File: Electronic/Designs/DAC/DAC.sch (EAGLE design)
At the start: 37 parts

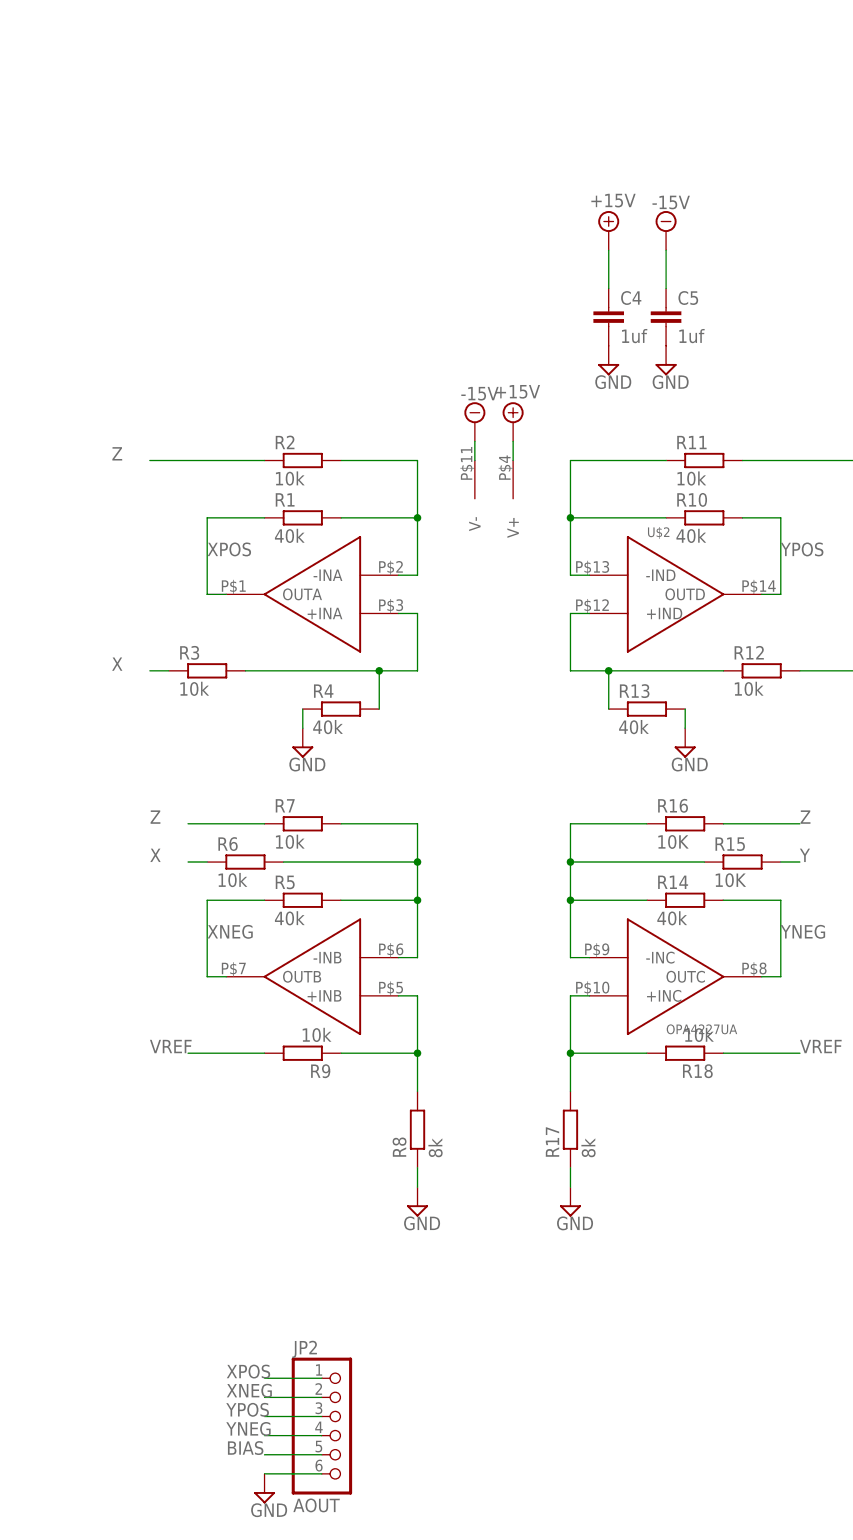
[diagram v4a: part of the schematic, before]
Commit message: improved dac board layout
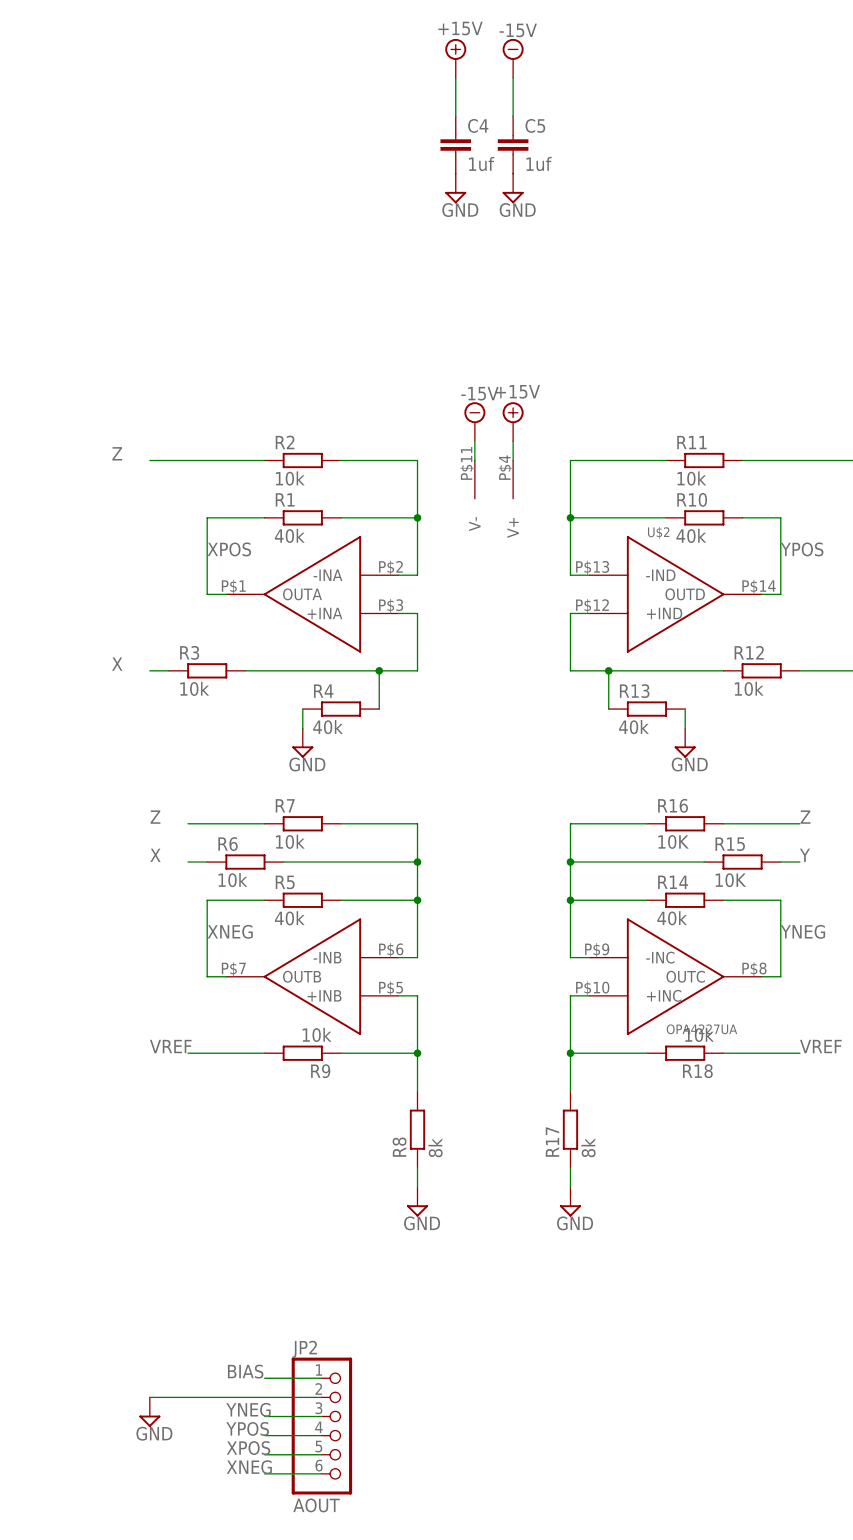
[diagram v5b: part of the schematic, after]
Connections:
- net BIAS: now also JP2.1; no longer JP2.5
- net GND: now also JP2.2; no longer JP2.6
- net XNEG: now also JP2.6; no longer JP2.2
- net XPOS: now also JP2.5; no longer JP2.1
- net YNEG: now also JP2.3; no longer JP2.4
- net YPOS: now also JP2.4; no longer JP2.3
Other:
- moved on the sheet: C4, C5
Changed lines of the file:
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@@
 <instance part="SUPPLY9" gate="GND" x="38.1" y="-50.8"/>
 <instance part="JP2" gate="A" x="99.06" y="-99.06"/>
-<instance part="SUPPLY10" gate="GND" x="88.9" y="-106.68"/>
+<instance part="SUPPLY10" gate="GND" x="73.66" y="-96.52"/>
 <instance part="JP3" gate="A" x="-50.8" y="0" rot="R180"/>
 <instance part="SUPPLY11" gate="GND" x="-40.64" y="-15.24"/>
@@
 <instance part="SUPPLY12" gate="GND" x="25.4" y="22.86"/>
 <instance part="SUPPLY13" gate="GND" x="33.02" y="22.86"/>
-<instance part="C4" gate="G$1" x="134.62" y="50.8"/>
-<instance part="C5" gate="G$1" x="142.24" y="50.8"/>
-<instance part="SUPPLY14" gate="GND" x="134.62" y="43.18"/>
-<instance part="SUPPLY15" gate="GND" x="142.24" y="43.18"/>
+<instance part="C4" gate="G$1" x="114.3" y="73.66"/>
+<instance part="C5" gate="G$1" x="121.92" y="73.66"/>
+<instance part="SUPPLY14" gate="GND" x="114.3" y="66.04"/>
+<instance part="SUPPLY15" gate="GND" x="121.92" y="66.04"/>
 <instance part="C6" gate="G$1" x="27.94" y="-30.48"/>
 <instance part="C7" gate="G$1" x="35.56" y="-30.48"/>
@@
 <instance part="SUPPLY22" gate="+5V" x="-88.9" y="83.82"/>
 <instance part="SUPPLY23" gate="+15V" x="-60.96" y="50.8"/>
-<instance part="SUPPLY24" gate="+15V" x="134.62" y="60.96"/>
-<instance part="SUPPLY25" gate="G$1" x="142.24" y="60.96" rot="R180"/>
+<instance part="SUPPLY24" gate="+15V" x="114.3" y="83.82"/>
+<instance part="SUPPLY25" gate="G$1" x="121.92" y="83.82" rot="R180"/>
 <instance part="SUPPLY26" gate="+15V" x="35.56" y="-15.24"/>
 <instance part="SUPPLY27" gate="G$1" x="27.94" y="-15.24" rot="R180"/>
@@
 <pinref part="SUPPLY25" gate="G$1" pin="-15V"/>
 <pinref part="C5" gate="G$1" pin="1"/>
-<wire x1="142.24" y1="58.42" x2="142.24" y2="53.34" width="0.1524" layer="91"/>
+<wire x1="121.92" y1="81.28" x2="121.92" y2="76.2" width="0.1524" layer="91"/>
 </segment>
 <segment>
@@
 <pinref part="SUPPLY24" gate="+15V" pin="+15V"/>
 <pinref part="C4" gate="G$1" pin="1"/>
-<wire x1="134.62" y1="58.42" x2="134.62" y2="53.34" width="0.1524" layer="91"/>
+<wire x1="114.3" y1="81.28" x2="114.3" y2="76.2" width="0.1524" layer="91"/>
 </segment>
 <segment>
@@
 <pinref part="R22" gate="G$1" pin="2"/>
 <wire x1="38.1" y1="-48.26" x2="33.02" y2="-48.26" width="0.1524" layer="91"/>
-</segment>
-<segment>
-<pinref part="JP2" gate="A" pin="6"/>
-<wire x1="96.52" y1="-104.14" x2="88.9" y2="-104.14" width="0.1524" layer="91"/>
-<pinref part="SUPPLY10" gate="GND" pin="GND"/>
 </segment>
 <segment>
@@
 <wire x1="-106.68" y1="22.86" x2="-96.52" y2="22.86" width="0.1524" layer="91"/>
 <wire x1="-96.52" y1="22.86" x2="-96.52" y2="20.32" width="0.1524" layer="91"/>
+</segment>
+<segment>
+<pinref part="JP2" gate="A" pin="2"/>
+<wire x1="96.52" y1="-93.98" x2="73.66" y2="-93.98" width="0.1524" layer="91"/>
+<pinref part="SUPPLY10" gate="GND" pin="GND"/>
 </segment>
 </net>
@@
 </segment>
 <segment>
-<pinref part="JP2" gate="A" pin="1"/>
-<wire x1="96.52" y1="-91.44" x2="88.9" y2="-91.44" width="0.1524" layer="91"/>
-<label x="83.82" y="-91.44" size="1.778" layer="95"/>
+<pinref part="JP2" gate="A" pin="5"/>
+<wire x1="96.52" y1="-101.6" x2="88.9" y2="-101.6" width="0.1524" layer="91"/>
+<label x="83.82" y="-101.6" size="1.778" layer="95"/>
 </segment>
 </net>
@@
 </segment>
 <segment>
-<pinref part="JP2" gate="A" pin="2"/>
-<wire x1="96.52" y1="-93.98" x2="88.9" y2="-93.98" width="0.1524" layer="91"/>
-<label x="83.82" y="-93.98" size="1.778" layer="95"/>
+<pinref part="JP2" gate="A" pin="6"/>
+<wire x1="96.52" y1="-104.14" x2="88.9" y2="-104.14" width="0.1524" layer="91"/>
+<label x="83.82" y="-104.14" size="1.778" layer="95"/>
 </segment>
 </net>
@@
 </segment>
 <segment>
-<pinref part="JP2" gate="A" pin="3"/>
-<wire x1="96.52" y1="-96.52" x2="88.9" y2="-96.52" width="0.1524" layer="91"/>
-<label x="83.82" y="-96.52" size="1.778" layer="95"/>
+<pinref part="JP2" gate="A" pin="4"/>
+<wire x1="96.52" y1="-99.06" x2="88.9" y2="-99.06" width="0.1524" layer="91"/>
+<label x="83.82" y="-99.06" size="1.778" layer="95"/>
 </segment>
 </net>
@@
 </segment>
 <segment>
-<pinref part="JP2" gate="A" pin="4"/>
-<wire x1="96.52" y1="-99.06" x2="88.9" y2="-99.06" width="0.1524" layer="91"/>
-<label x="83.82" y="-99.06" size="1.778" layer="95"/>
+<pinref part="JP2" gate="A" pin="3"/>
+<wire x1="96.52" y1="-96.52" x2="88.9" y2="-96.52" width="0.1524" layer="91"/>
+<label x="83.82" y="-96.52" size="1.778" layer="95"/>
 </segment>
 </net>
@@
 </segment>
 <segment>
-<pinref part="JP2" gate="A" pin="5"/>
-<wire x1="96.52" y1="-101.6" x2="88.9" y2="-101.6" width="0.1524" layer="91"/>
-<label x="83.82" y="-101.6" size="1.778" layer="95"/>
-</segment>
-</net>
+<pinref part="JP2" gate="A" pin="1"/>
+<wire x1="96.52" y1="-91.44" x2="88.9" y2="-91.44" width="0.1524" layer="91"/>
+<label x="83.82" y="-91.44" size="1.778" layer="95"/>
+</segment>
+</net>

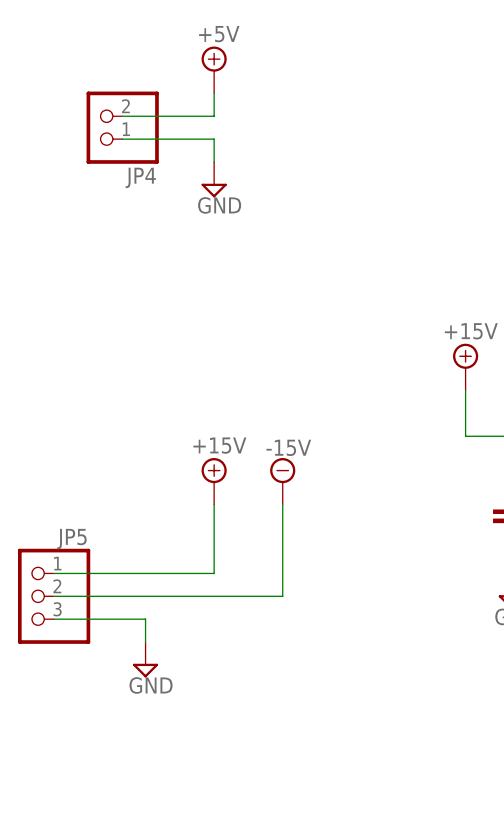
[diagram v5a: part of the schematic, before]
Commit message: Added to dac pcb finished routing
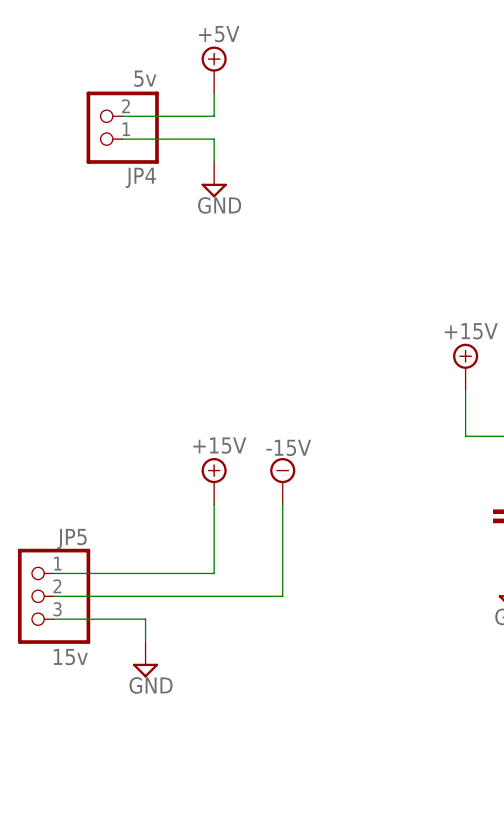
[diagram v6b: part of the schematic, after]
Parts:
- JP4: value (none) -> 5v
- JP5: value (none) -> 15v
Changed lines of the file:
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@@
 <part name="SUPPLY30" library="supply2" deviceset="+15V" device=""/>
 <part name="SUPPLY31" library="supply2" deviceset="-15V" device=""/>
-<part name="JP4" library="pinhead" deviceset="PINHD-1X2" device=""/>
-<part name="JP5" library="pinhead" deviceset="PINHD-1X3" device=""/>
+<part name="JP4" library="pinhead" deviceset="PINHD-1X2" device="" value="5v"/>
+<part name="JP5" library="pinhead" deviceset="PINHD-1X3" device="" value="15v"/>
 <part name="SUPPLY32" library="supply2" deviceset="GND" device=""/>
 </parts>
